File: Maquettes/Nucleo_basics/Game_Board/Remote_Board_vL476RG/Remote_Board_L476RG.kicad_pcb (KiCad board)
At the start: 2 copper layers, 159.6 x 122 mm, 43 parts, among them CON1 MikroE-nRF-S-module, J1 LCD_SD, J10 3.3V_reg, J2 JoyStick, J3 AnalogIn, J4 BAT_IN, J5 Morpho_Gauche, J6 Morpho_Droite, J8 I2C_EXT, J9 GND_reg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

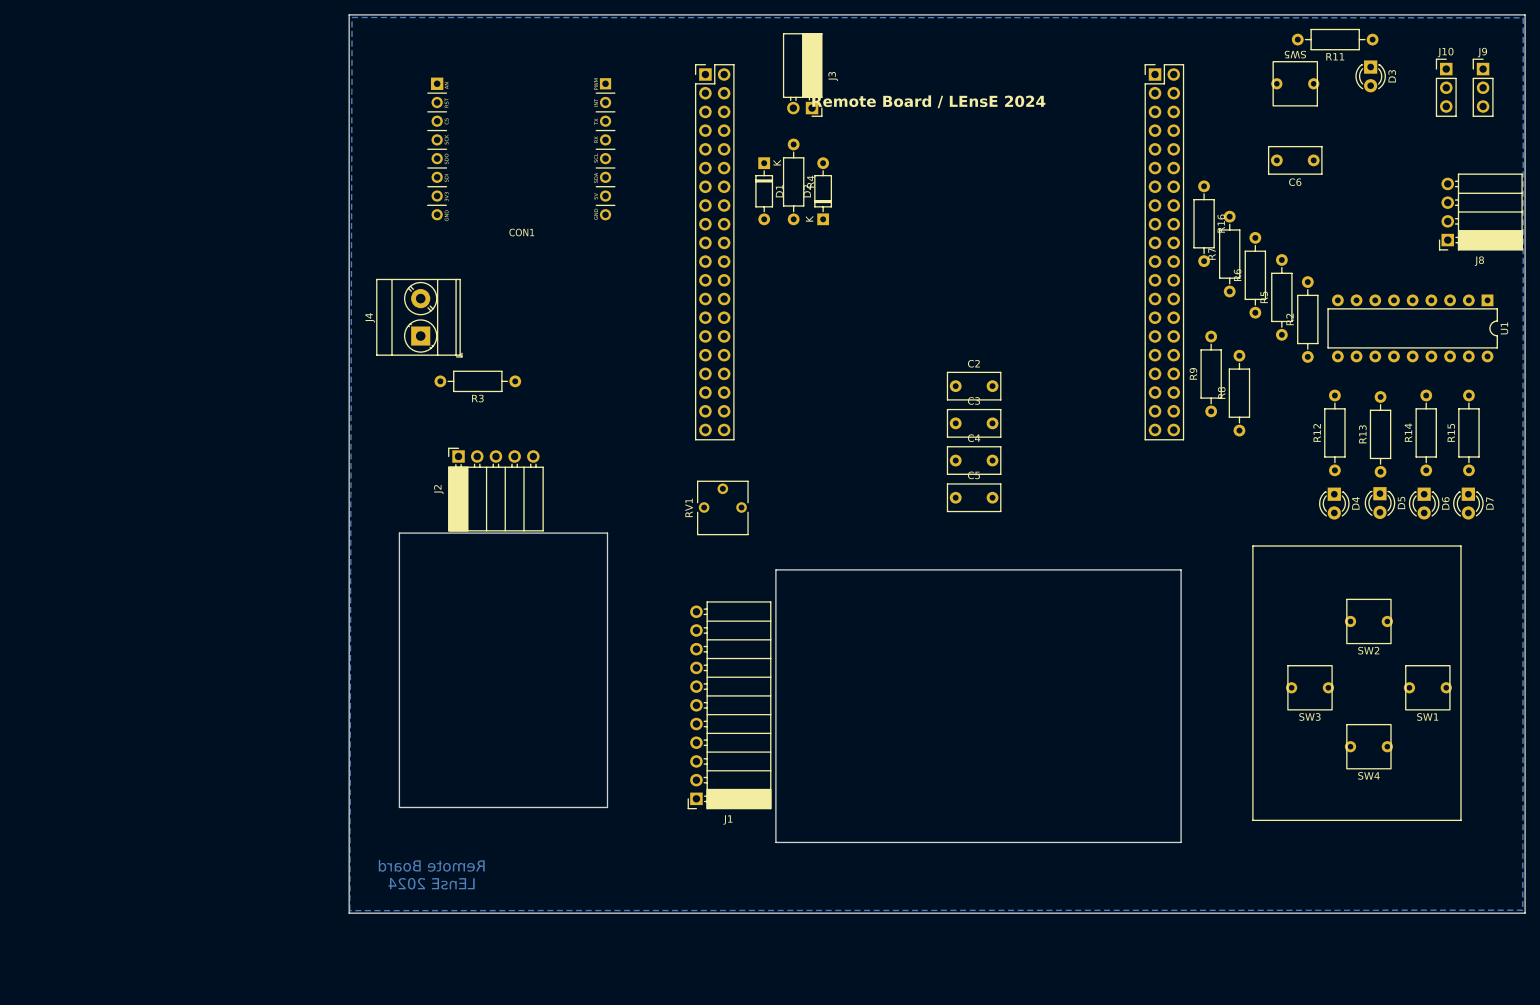
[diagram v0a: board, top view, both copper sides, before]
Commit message: Update Remote Board / L476RG version
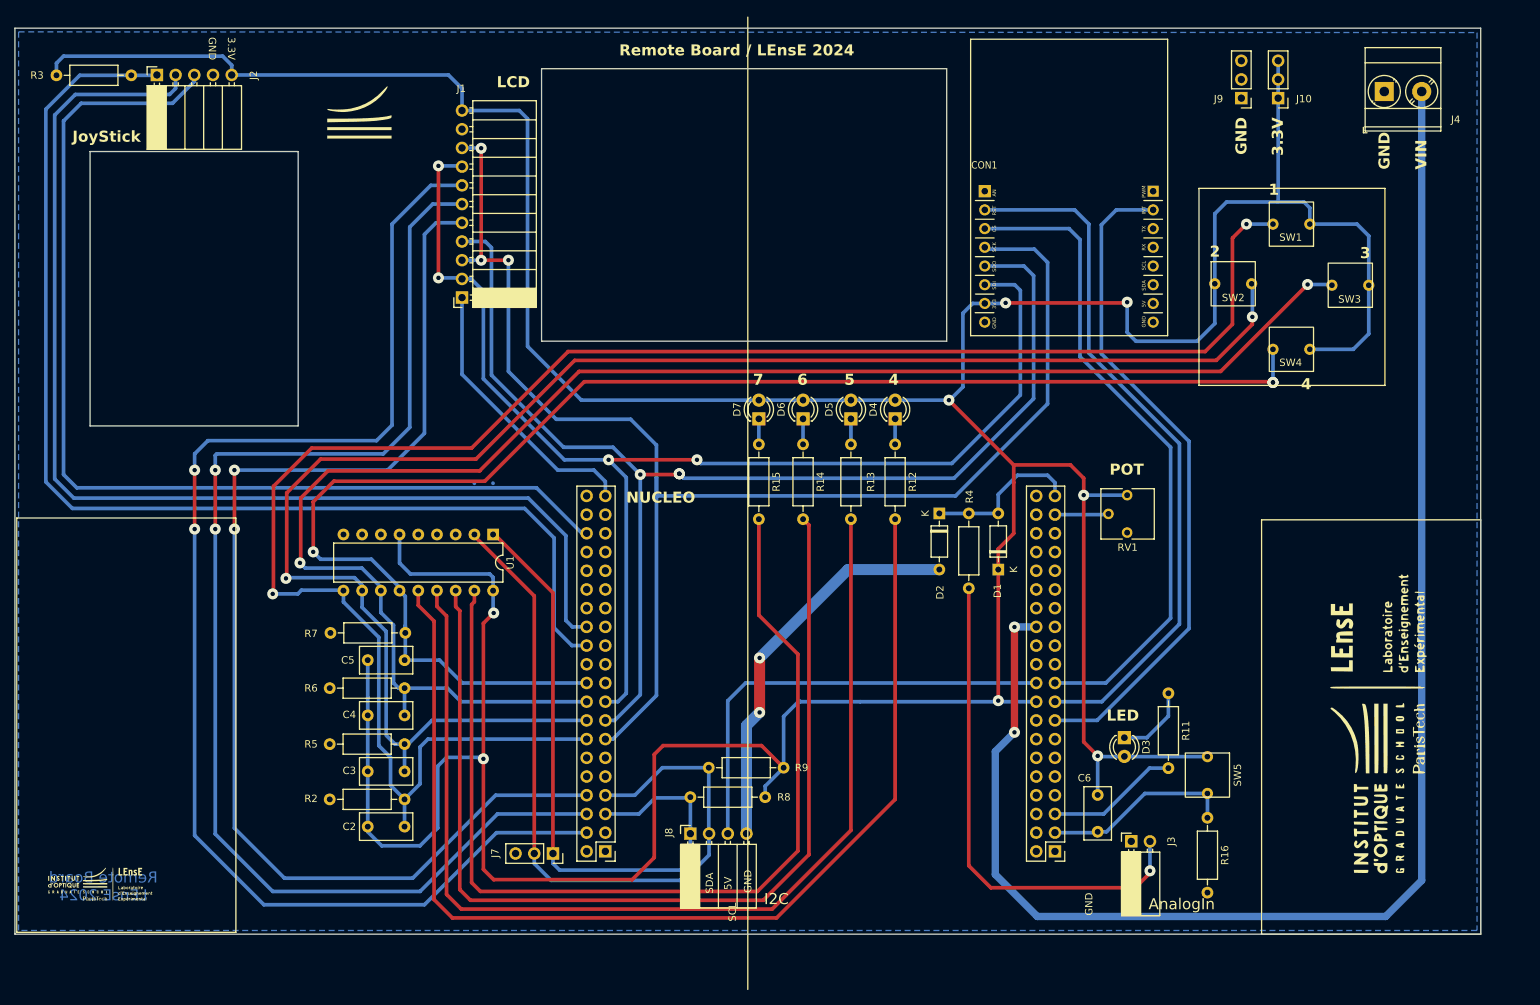
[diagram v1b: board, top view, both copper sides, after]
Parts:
- added G***: LOGO, LEnsE_devices:Logo_Alone, F.Cu at (122.8, 41.4)
- added G***: LOGO, LEnsE_devices:Logo_Big, F.Cu at (260.4, 124.4)
- added G***: LOGO, LEnsE_devices:Logo_Small, F.Cu at (87.6, 146.0)
- added J7: I2C_Visu, Connector_PinSocket_2.54mm:PinSocket_1x03_P2.54mm_Vertical, F.Cu at (149.1, 142.1)
- CON1: value MikroE-nRF-S-module -> nRF-S/T
- moved U1 138.7 mm to (140.9, 98.7)
- moved R2 136.5 mm to (128.9, 134.7), turned to 180 degrees
- moved J4 135.0 mm to (261.9, 38.6), turned to 0 degrees
- moved R5 131.4 mm to (128.9, 127.2), turned to 180 degrees
- moved J8 130.6 mm to (167.7, 139.3), turned to 90 degrees
- moved J6 129.2 mm to (156.2, 141.8), turned to 180 degrees
- moved R6 126.3 mm to (128.9, 119.6), turned to 180 degrees
- moved R7 121.1 mm to (129.0, 112.1), turned to 180 degrees
- moved J5 115.7 mm to (217.2, 141.8), turned to 180 degrees
- moved J3 108.6 mm to (227.6, 140.4), turned to 90 degrees
- moved C2 99.7 mm to (123.9, 138.4)
- moved SW5 99.7 mm to (233.4, 131.4), turned to -90 degrees
- moved D3 97.0 mm to (226.6, 126.3)
- moved D7 96.9 mm to (177.0, 83.0), turned to 90 degrees
- moved R15 96.5 mm to (177.0, 86.5), turned to -90 degrees
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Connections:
- D1 pad 1: VCC -> 3.3V_NUC
- J5 pad 15: LCD_DC -> nRF_INT
- J5 pad 17: LCD_RES -> nRF_CE
- J5 pad 19: LCD_CS -> nRF_CS
- J5 pad 3: T_OUT -> SW5_OUT
- J5 pad 33: JOYSW -> unconnected-(J5-Pin_33-Pad33)
- J5 pad 37: JOYX -> POT_OUT
- J5 pad 38: AN_IN -> unconnected-(J5-Pin_38-Pad38)
- J5 pad 39: JOYY -> AN_IN
- J5 pad 40: POT_OUT -> unconnected-(J5-Pin_40-Pad40)
- J5 pad 5: SD_CS -> LED_OUT
- J6 pad 14: SW4_OUT -> SW1_OUT
- J6 pad 16: SW3_OUT -> SW2_OUT
- J6 pad 18: SW2_OUT -> SW3_OUT
- J6 pad 20: SW1_OUT -> SW4_OUT
- J6 pad 21: nRF_CS -> unconnected-(J6-Pin_21-Pad21)
- J6 pad 23: nRF_INT -> unconnected-(J6-Pin_23-Pad23)
- J6 pad 24: unconnected-(J6-Pin_24-Pad24) -> JOYSW
- J6 pad 25: nRF_CE -> unconnected-(J6-Pin_25-Pad25)
- J6 pad 26: unconnected-(J6-Pin_26-Pad26) -> JOYY
- J6 pad 28: MCP_INT -> unconnected-(J6-Pin_28-Pad28)
- J6 pad 30: SDA -> unconnected-(J6-Pin_30-Pad30)
- J6 pad 32: SCL -> unconnected-(J6-Pin_32-Pad32)
- J6 pad 36: unconnected-(J6-Pin_36-Pad36) -> JOYX
- J6 pad 39: unconnected-(J6-Pin_39-Pad39) -> SD_CS
- J6 pad 4: LED_OUT -> LCD_DC
- J6 pad 5: unconnected-(J6-Pin_5-Pad5) -> SCL
- J6 pad 6: unconnected-(J6-Pin_6-Pad6) -> LCD_RES
- J6 pad 7: unconnected-(J6-Pin_7-Pad7) -> SDA
- J6 pad 8: SW5_OUT -> LCD_CS
- RV1 pad 1: VCC -> 3.3V_NUC
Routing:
- net 3.3V_NUC: track 0.00 -> 630.3 mm, vias 0 -> 8
- net SW1_OUT: track 0.00 -> 248.3 mm, vias 0 -> 2
- net SW2_OUT: track 0.00 -> 223.0 mm, vias 0 -> 2
- net SW3_OUT: track 0.00 -> 218.1 mm, vias 0 -> 2
- net VIN: track 0.00 -> 207.0 mm, vias 0 -> 2
- net SW4_OUT: track 0.00 -> 199.6 mm, vias 0 -> 3
- net SCK: track 0.00 -> 196.9 mm, vias 0 -> 3
- net LCD_DC: track 0.00 -> 180.4 mm, vias 0 -> 2
- net MOSI: track 0.00 -> 174.6 mm, vias 0 -> 4
- net LCD_RES: track 0.00 -> 173.0 mm, vias 0 -> 2
- net MISO: track 0.00 -> 165.6 mm, vias 0 -> 3
- net LCD_CS: track 0.00 -> 164.5 mm, vias 0 -> 2
- net JOYSW: track 0.00 -> 157.5 mm
- net JOYY: track 0.00 -> 156.4 mm
- net LED1: track 0.00 -> 151.2 mm
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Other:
- board size 159.6 x 122 mm -> 199 x 123 mm
- board text added: "1"
- board text added: "2"
- board text added: "3"
- board text added: "3.3V"
- board text added: "4"
- board text added: "5"
- board text added: "5V"
- board text added: "6"
- board text added: "7"
- board text added: "AnalogIn"
- board text added: "GND"
- board text added: "I2C"
- board text added: "JoyStick"
- board text added: "LCD"
- board text added: "LED"
- board text added: "NUCLEO"
- board text added: "POT"
- board text added: "SCL"
- board text added: "SDA"
- board text added: "VIN"

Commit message: Update Remote Board / L476RG
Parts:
- CON1: value nRF-S/T -> MikroE-nRF-S-module
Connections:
- J6 pad 32: unconnected-(J6-Pin_32-Pad32) -> MCP_INT
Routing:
- net MCP_INT: track 0.00 -> 54.0 mm, vias 0 -> 2

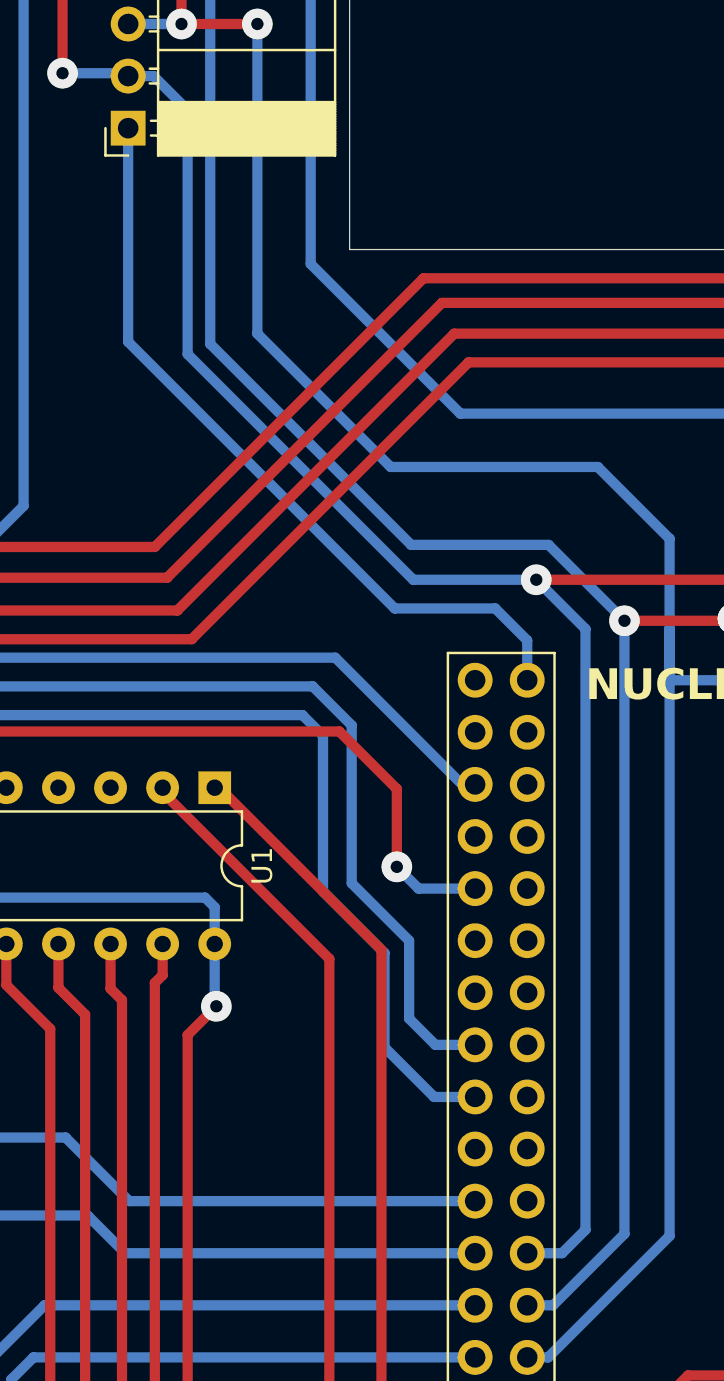
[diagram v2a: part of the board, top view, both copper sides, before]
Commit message: Update Remote and Robot Nucleo basics
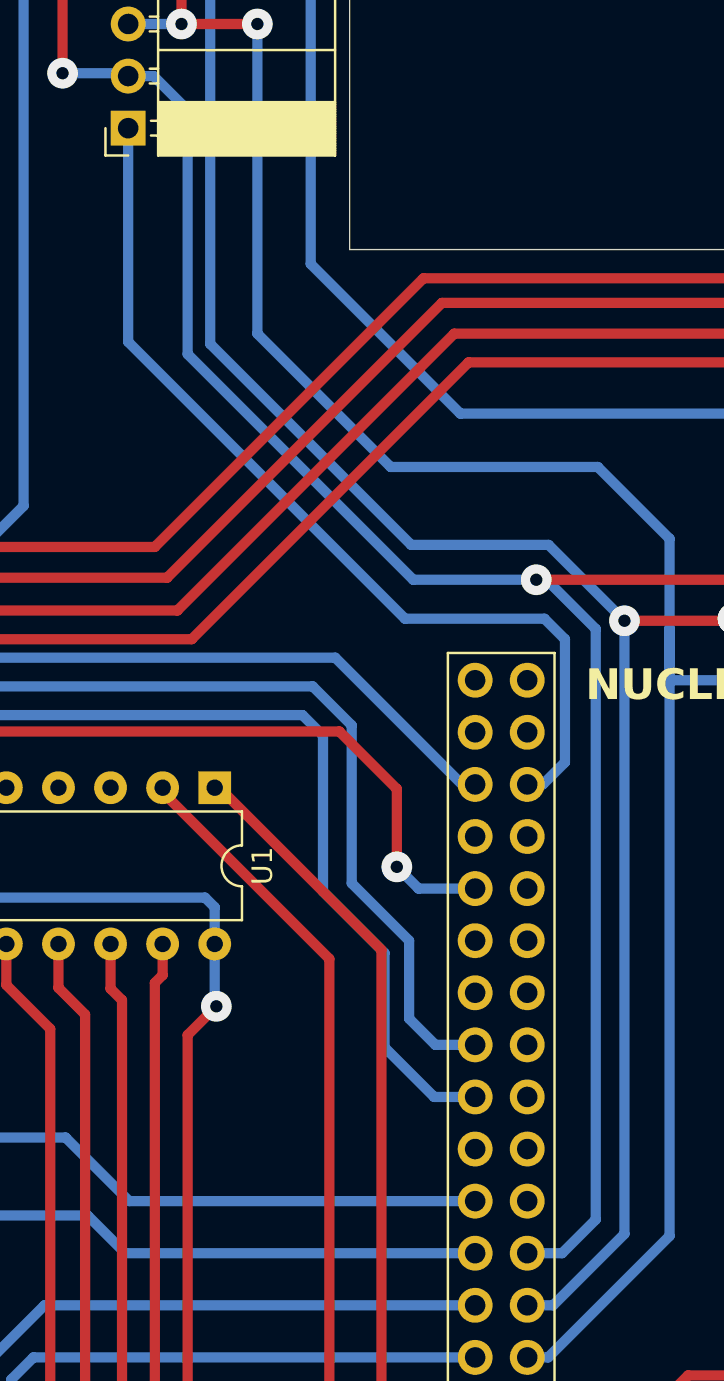
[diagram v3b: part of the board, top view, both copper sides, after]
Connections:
- J6 pad 35: unconnected-(J6-Pin_35-Pad35) -> SD_CS
- J6 pad 39: SD_CS -> unconnected-(J6-Pin_39-Pad39)
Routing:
- net SD_CS: track 37.9 -> 46.0 mm
- net MOSI: track 174.6 -> 175.3 mm
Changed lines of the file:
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@@
 	(net 72 "unconnected-(J6-Pin_9-Pad9)")
 	(net 73 "unconnected-(J6-Pin_34-Pad34)")
-	(net 74 "unconnected-(J6-Pin_35-Pad35)")
+	(net 74 "unconnected-(J6-Pin_39-Pad39)")
 	(net 75 "unconnected-(J6-Pin_12-Pad12)")
 	(net 76 "MCP_INT")
@@
 			(layers "*.Cu" "*.Mask")
 			(remove_unused_layers no)
-			(net 74 "unconnected-(J6-Pin_35-Pad35)")
+			(net 25 "SD_CS")
 			(pinfunction "Pin_35")
 			(pintype "passive")
@@
 			(layers "*.Cu" "*.Mask")
 			(remove_unused_layers no)
-			(net 25 "SD_CS")
+			(net 74 "unconnected-(J6-Pin_39-Pad39)")
 			(pinfunction "Pin_39")
 			(pintype "passive")
@@
 	)
 	(segment
-		(start 154.6 90)
-		(end 149.7 90)
+		(start 158 97.5)
+		(end 156.92 98.58)
 		(width 0.5)
 		(layer "B.Cu")
@@
 	)
 	(segment
-		(start 156.160001 91.560001)
-		(end 154.6 90)
+		(start 156.92 98.58)
+		(end 156.160001 98.58)
 		(width 0.5)
 		(layer "B.Cu")
@@
 	)
 	(segment
-		(start 156.160001 93.5)
-		(end 156.160001 91.560001)
+		(start 157 90.5)
+		(end 158 91.5)
 		(width 0.5)
 		(layer "B.Cu")
@@
 	(segment
 		(start 136.7 77)
-		(end 136.7 66.58)
+		(end 150.2 90.5)
+		(width 0.5)
+		(layer "B.Cu")
+		(net 25)
+	)
+	(segment
+		(start 150.2 90.5)
+		(end 157 90.5)
+		(width 0.5)
+		(layer "B.Cu")
+		(net 25)
+	)
+	(segment
+		(start 158 91.5)
+		(end 158 97.5)
 		(width 0.5)
 		(layer "B.Cu")
@@
 	)
 	(segment
-		(start 149.7 90)
+		(start 136.7 66.58)
 		(end 136.7 77)
 		(width 0.5)
@@
 	)
 	(segment
-		(start 159 120.3)
-		(end 159 91)
-		(width 0.5)
-		(layer "B.Cu")
-		(net 41)
-	)
-	(segment
 		(start 133.5 63.9)
 		(end 136.56 63.9)
@@
 	)
 	(segment
+		(start 159.5 119.8)
+		(end 159.5 91)
+		(width 0.5)
+		(layer "B.Cu")
+		(net 41)
+	)
+	(segment
 		(start 212.5 79.8)
 		(end 212.5 65.6)
@@
 	)
 	(segment
-		(start 157.86 121.44)
-		(end 159 120.3)
+		(start 156.160001 121.44)
+		(end 157.86 121.44)
 		(width 0.5)
 		(layer "B.Cu")
@@
 	)
 	(segment
-		(start 156.160001 121.44)
-		(end 157.86 121.44)
+		(start 211.73 64.83)
+		(end 207.67 64.83)
 		(width 0.5)
 		(layer "B.Cu")
@@
 	)
 	(segment
-		(start 211.73 64.83)
-		(end 207.67 64.83)
+		(start 136.6 48.7)
+		(end 136.7 48.8)
 		(width 0.5)
 		(layer "B.Cu")
@@
 	)
 	(segment
-		(start 136.6 48.7)
-		(end 136.7 48.8)
+		(start 157.1 88.6)
+		(end 156.6 88.6)
+		(width 0.5)
+		(layer "B.Cu")
+		(net 41)
+	)
+	(segment
+		(start 159.5 91)
+		(end 157.1 88.6)
 		(width 0.5)
 		(layer "B.Cu")
@@
 	)
 	(segment
-		(start 159 91)
-		(end 156.6 88.6)
+		(start 157.86 121.44)
+		(end 159.5 119.8)
 		(width 0.5)
 		(layer "B.Cu")

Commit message: Update Remote and Robot Boards
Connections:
- J5 pad 15: nRF_INT -> unconnected-(J5-Pin_15-Pad15)
- J5 pad 17: nRF_CE -> nRF_INT
- J5 pad 19: nRF_CS -> nRF_CE
- J5 pad 23: unconnected-(J5-Pin_23-Pad23) -> nRF_CS
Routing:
- net nRF_CS: track 89.4 -> 85.0 mm
- net nRF_INT: track 91.0 -> 89.9 mm
- net nRF_CE: track 95.6 -> 94.5 mm
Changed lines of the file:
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@@
 	(net 56 "unconnected-(J5-Pin_4-Pad4)")
 	(net 57 "unconnected-(J5-Pin_29-Pad29)")
-	(net 58 "unconnected-(J5-Pin_23-Pad23)")
+	(net 58 "unconnected-(J5-Pin_15-Pad15)")
 	(net 59 "POT_OUT")
 	(net 60 "unconnected-(J6-Pin_19-Pad19)")
@@
 			(layers "*.Cu" "*.Mask")
 			(remove_unused_layers no)
-			(net 14 "nRF_INT")
+			(net 58 "unconnected-(J5-Pin_15-Pad15)")
 			(pinfunction "Pin_15")
 			(pintype "passive")
@@
 			(layers "*.Cu" "*.Mask")
 			(remove_unused_layers no)
-			(net 13 "nRF_CE")
+			(net 14 "nRF_INT")
 			(pinfunction "Pin_17")
 			(pintype "passive")
@@
 			(layers "*.Cu" "*.Mask")
 			(remove_unused_layers no)
-			(net 9 "nRF_CS")
+			(net 13 "nRF_CE")
 			(pinfunction "Pin_19")
 			(pintype "passive")
@@
 			(layers "*.Cu" "*.Mask")
 			(remove_unused_layers no)
-			(net 58 "unconnected-(J5-Pin_23-Pad23)")
+			(net 9 "nRF_CS")
 			(pinfunction "Pin_23")
 			(pintype "passive")
@@
 	)
 	(segment
-		(start 220.6 74.6)
-		(end 232.9 86.9)
+		(start 217.2 113.82)
+		(end 225.28 113.82)
 		(width 0.5)
 		(layer "B.Cu")
@@
 	)
 	(segment
-		(start 219.11 57.21)
-		(end 220.6 58.7)
+		(start 232.9 86.9)
+		(end 232.9 106.2)
 		(width 0.5)
 		(layer "B.Cu")
@@
 	)
 	(segment
-		(start 207.67 57.21)
-		(end 219.11 57.21)
+		(start 220.6 74.6)
+		(end 232.9 86.9)
 		(width 0.5)
 		(layer "B.Cu")
@@
 	)
 	(segment
-		(start 224.1 118.9)
-		(end 217.2 118.9)
+		(start 225.28 113.82)
+		(end 232.9 106.2)
 		(width 0.5)
 		(layer "B.Cu")
@@
 	)
 	(segment
-		(start 232.9 110.1)
-		(end 224.1 118.9)
+		(start 219.11 57.21)
+		(end 220.6 58.7)
 		(width 0.5)
 		(layer "B.Cu")
@@
 	)
 	(segment
-		(start 232.9 86.9)
-		(end 232.9 110.1)
+		(start 207.67 57.21)
+		(end 219.11 57.21)
 		(width 0.5)
 		(layer "B.Cu")
@@
 	)
 	(segment
+		(start 226.1 118.9)
+		(end 228.3 116.7)
+		(width 0.5)
+		(layer "B.Cu")
+		(net 13)
+	)
+	(segment
 		(start 221.8 74.1)
 		(end 221.8 56.6)
@@
 	)
 	(segment
+		(start 228.3 116.7)
+		(end 234.1 110.9)
+		(width 0.5)
+		(layer "B.Cu")
+		(net 13)
+	)
+	(segment
 		(start 219.87 54.67)
 		(end 207.67 54.67)
@@
 	)
 	(segment
-		(start 223.56 121.44)
-		(end 234.1 110.9)
-		(width 0.5)
-		(layer "B.Cu")
-		(net 13)
-	)
-	(segment
-		(start 217.2 121.44)
-		(end 223.56 121.44)
+		(start 217.2 118.9)
+		(end 226.1 118.9)
 		(width 0.5)
 		(layer "B.Cu")
@@
 	)
 	(segment
-		(start 222.92 123.98)
+		(start 227.85 119.05)
 		(end 235.4 111.5)
 		(width 0.5)
@@
 	)
 	(segment
-		(start 217.2 123.98)
-		(end 222.92 123.98)
+		(start 217.2 121.44)
+		(end 225.46 121.44)
 		(width 0.5)
 		(layer "B.Cu")
@@
 		(width 0.5)
 		(layer "B.Cu")
+		(net 14)
+	)
+	(segment
+		(start 225.46 121.44)
+		(end 227.85 119.05)
+		(width 0.5)
+		(layer "B.Cu")

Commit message: Update Boards
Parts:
- RV1: value R_10k -> R_Potentiometer
- moved RV1 0.07 mm to (227.0, 93.5)
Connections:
- J6 pad 18: SW3_OUT -> unconnected-(J6-Pin_18-Pad18)
- J6 pad 20: SW4_OUT -> unconnected-(J6-Pin_20-Pad20)
- J6 pad 23: unconnected-(J6-Pin_23-Pad23) -> SW3_OUT
- J6 pad 25: unconnected-(J6-Pin_25-Pad25) -> SW4_OUT
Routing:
- net SW3_OUT: track 218.1 -> 238.9 mm, vias 2 -> 3
- net SW4_OUT: track 199.6 -> 213.1 mm, vias 3 -> 4
- net MISO: track 165.6 -> 171.5 mm
- net SD_CS: track 46.0 -> 49.1 mm
- net MOSI: track 175.3 -> 177.4 mm
- net SCK: track 196.9 -> 198.0 mm

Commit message: Update Robot and Remote Boards
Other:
- board text added: "00h IODIR 01h IPOL 02h GPINTEN 03h DEFVAL 04h INTCON 05h IOCON 06h GPPU 07h INTF 08h INTCAP (Read-only) 09h GPIO 0Ah OLAT"
- board text added: "MCP23008 / ADD = 0x20"
- board text added: "X"
- board text added: "nRF S/T module"
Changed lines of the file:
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@@
+		)
+	)
+	(gr_text "00h IODIR\n01h IPOL\n02h GPINTEN\n03h DEFVAL\n04h INTCON\n05h IOCON\n06h GPPU\n07h INTF\n08h INTCAP (Read-only)\n09h GPIO\n0Ah OLAT"
+		(at 80.05 118.95 0)
+		(layer "F.SilkS")
+		(effects
+			(font
+				(size 1 1)
+				(thickness 0.15)
+			)
+			(justify left bottom)
 		)
 	)
@@
 		)
 	)
+	(gr_text "MCP23008 / ADD = 0x20"
+		(at 77.6 99.6 0)
+		(layer "F.SilkS")
+		(effects
+			(font
+				(size 1 1)
+				(thickness 0.15)
+			)
+			(justify left bottom)
+		)
+	)
 	(gr_text "7"
 		(at 176.2 78.6 0)
@@
 		)
 	)
+	(gr_text "X"
+		(at 158.4 142.45 0)
+		(layer "F.SilkS")
+		(effects
+			(font
+				(size 1 1)
+				(thickness 0.15)
+			)
+			(justify left bottom)
+		)
+	)
 	(gr_text "JoyStick"
 		(at 83.8 45.6 0)
@@
 		)
 	)
+	(gr_text "X"
+		(at 219.8 142.4 0)
+		(layer "F.SilkS")
+		(effects
+			(font
+				(size 1 1)
+				(thickness 0.15)
+			)
+			(justify left bottom)
+		)
+	)
 	(gr_text "GND"
 		(at 176.1 147.4 90)
@@
 		)
 	)
+	(gr_text "MCP23008 / ADD = 0x20"
+		(at 119 96.8 0)
+		(layer "F.SilkS")
+		(effects
+			(font
+				(size 1 1)
+				(thickness 0.15)
+			)
+			(justify left bottom)
+		)
+	)
 	(gr_text "POT"
 		(at 224.6 90.8 0)
@@
 		)
 	)
+	(gr_text "nRF S/T module"
+		(at 218.85 34.4 0)
+		(layer "F.SilkS")
+		(effects
+			(font
+				(size 1 1)
+				(thickness 0.15)
+			)
+			(justify left bottom)
+		)
+	)
 	(gr_text "5V"
 		(at 173.4 147 90)
@@
 			)
 			(justify left bottom)
+		)
+	)
+	(gr_text "X"
+		(at 210.95 142.45 0)
+		(layer "F.SilkS")
+		(effects
+			(font
+				(size 1 1)
+				(thickness 0.15)
+			)
+			(justify left bottom)
